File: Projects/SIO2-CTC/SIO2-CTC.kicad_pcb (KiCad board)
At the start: 2 copper layers, 100 x 80 mm, 12 parts, among them IC1 MCP2221-I_P, J1 RetroZ-SBC_ClientBus, J2 Conn_01x08, J3 USB_OTG, U1 74LS138, U2 Z84C3008PEG, U3 Z84C40

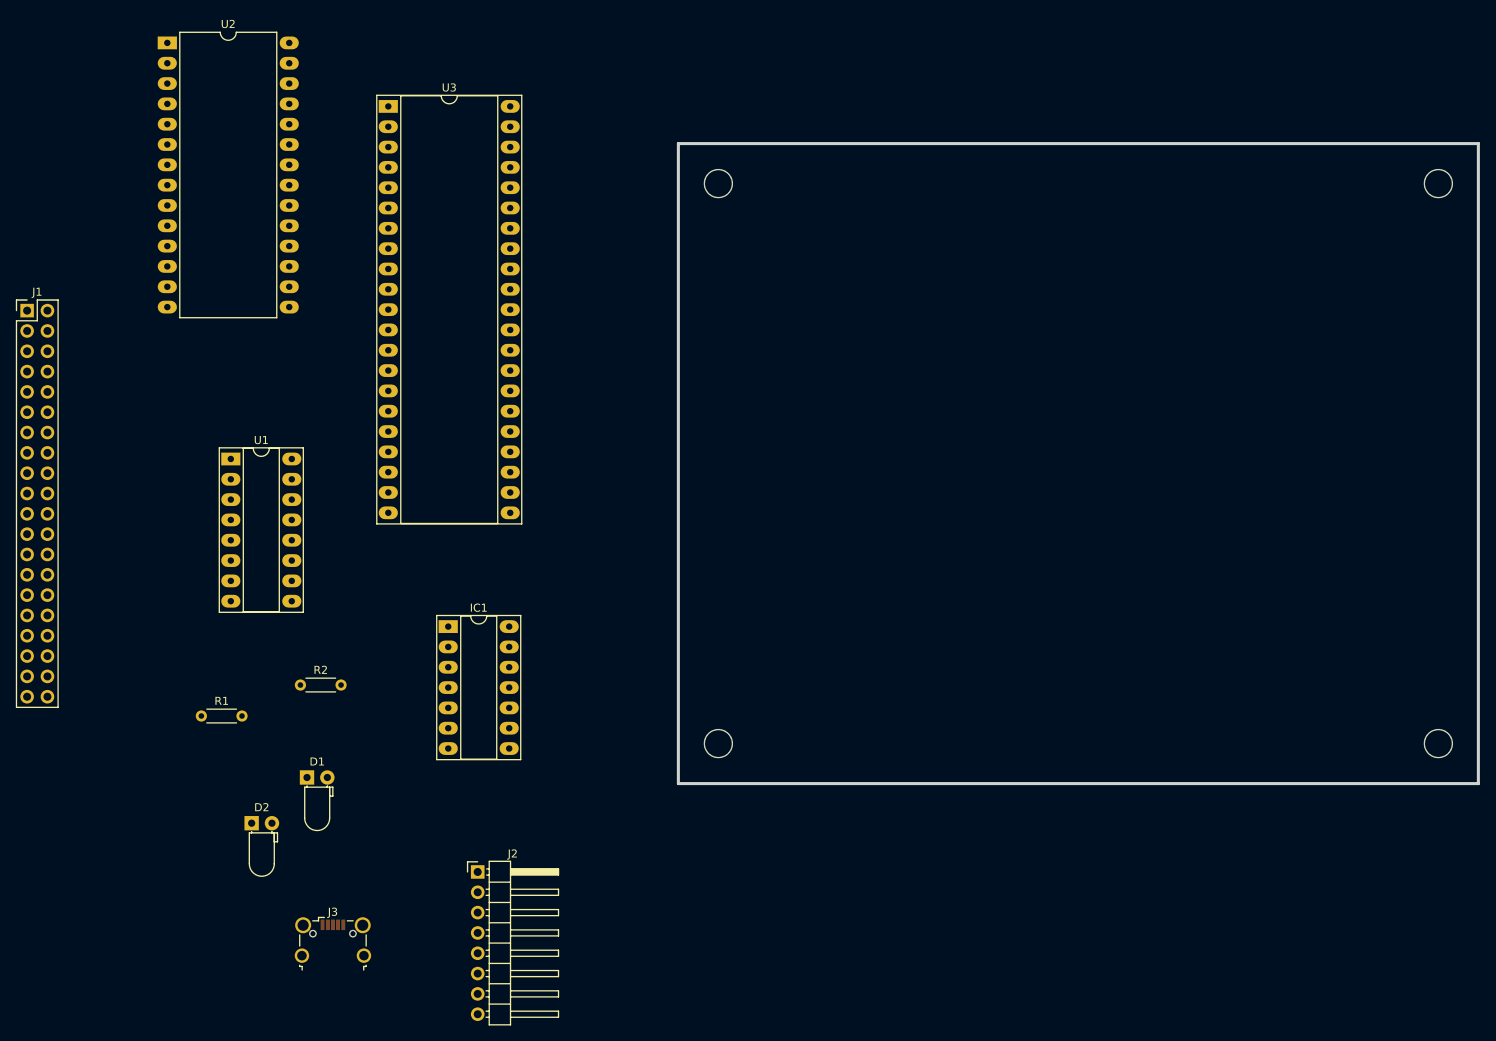
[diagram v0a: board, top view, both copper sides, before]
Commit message: added usb to serial with an FT230XS-U chip
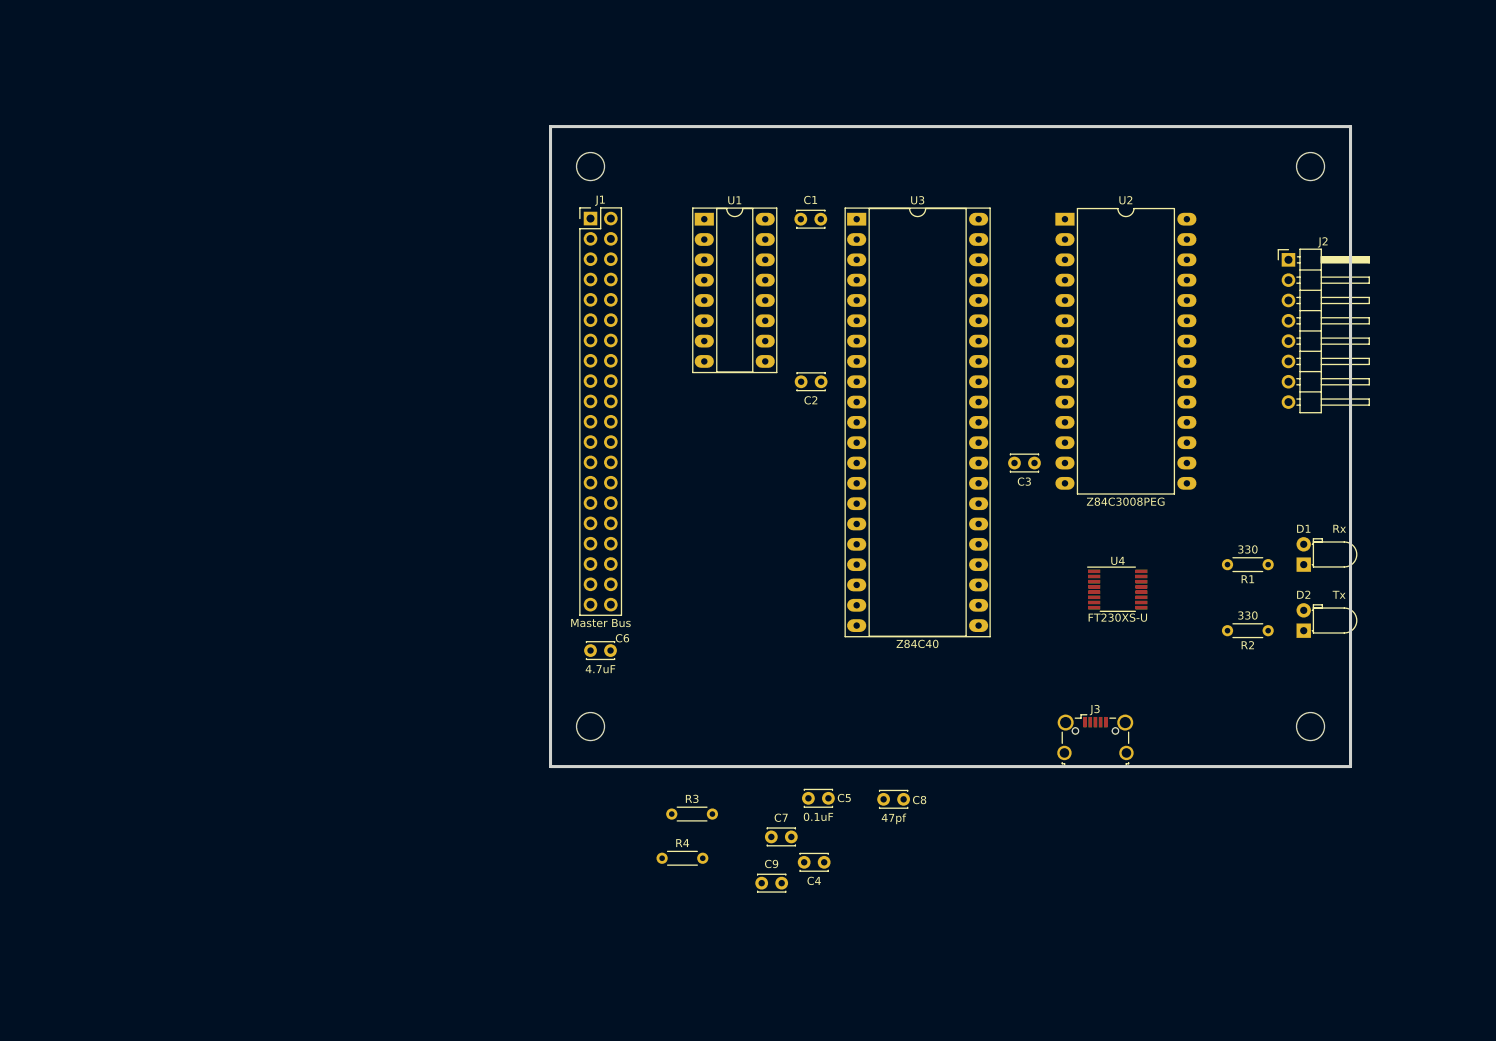
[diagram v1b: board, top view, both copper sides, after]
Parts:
- removed IC1: MCP2221-I_P, Housings_DIP:DIP-14_W7.62mm_Socket_LongPads
- added C1: 0.1uF, Capacitors_THT:C_Disc_D3.4mm_W2.1mm_P2.50mm, F.Cu at (121.3, 68.6)
- added C2: 0.1uF, Capacitors_THT:C_Disc_D3.4mm_W2.1mm_P2.50mm, F.Cu at (123.8, 88.9)
- added C3: 0.1uF, Capacitors_THT:C_Disc_D3.4mm_W2.1mm_P2.50mm, F.Cu at (150.5, 99.1)
- added C4: 0.1uF, Capacitors_THT:C_Disc_D3.4mm_W2.1mm_P2.50mm, F.Cu at (124.2, 149.0)
- added C5: 0.1uF, Capacitors_THT:C_Disc_D3.4mm_W2.1mm_P2.50mm, F.Cu at (122.2, 141.0)
- added C6: 4.7uF, Capacitors_THT:C_Disc_D3.4mm_W2.1mm_P2.50mm, F.Cu at (95.0, 122.5)
- added C7: 0.1uF, Capacitors_THT:C_Disc_D3.4mm_W2.1mm_P2.50mm, F.Cu at (117.6, 145.8)
- added C8: 47pf, Capacitors_THT:C_Disc_D3.4mm_W2.1mm_P2.50mm, F.Cu at (131.6, 141.1)
- added C9: 47pf, Capacitors_THT:C_Disc_D3.4mm_W2.1mm_P2.50mm, F.Cu at (116.4, 151.6)
- added R3: 27, Resistors_THT:R_Axial_DIN0204_L3.6mm_D1.6mm_P5.08mm_Horizontal, F.Cu at (105.2, 142.9)
- added R4: 27, Resistors_THT:R_Axial_DIN0204_L3.6mm_D1.6mm_P5.08mm_Horizontal, F.Cu at (103.9, 148.5)
- added U4: FT230XS-U, Housings_SSOP:TSSOP-16_4.4x5mm_Pitch0.65mm, F.Cu at (160.9, 114.9)
- J1: value RetroZ-SBC_ClientBus -> Master Bus
- moved R1 134.7 mm to (179.7, 111.8), turned to 180 degrees
- moved D2 133.7 mm to (184.2, 120.0), turned to 90 degrees
- moved D1 127.4 mm to (184.2, 111.8), turned to 90 degrees
- moved J2 127.0 mm to (182.2, 73.7)
- moved R2 121.2 mm to (179.7, 120.0), turned to 180 degrees
- moved U2 114.3 mm to (154.3, 68.6)
- moved J3 98.6 mm to (158.1, 133.3)
- moved J1 71.4 mm to (95.0, 68.5)
- moved U1 66.3 mm to (109.2, 68.6)
- moved U3 60.2 mm to (128.3, 68.6)
- moved REF** 16.1 mm to (90.0, 137.0)
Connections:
- J2 pad 2: /GPIO2 -> /CBUS0
- J2 pad 3: /GPIO3 -> /CBUS3
- J3 pad 2: Net-(IC1-Pad12) -> /D-
- J3 pad 3: Net-(IC1-Pad13) -> /D+
- R1 pad 2: Net-(IC1-Pad2) -> /RxLED
- R2 pad 2: Net-(IC1-Pad3) -> /TxLED
- U3 pad 12: Net-(IC1-Pad6) -> /RxA
- U3 pad 15: Net-(IC1-Pad5) -> /TxA
- U3 pad 17: Net-(U3-Pad17) -> /~RTSA
- U3 pad 18: Net-(U3-Pad18) -> /~CTSA
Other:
- net class Default: clearance 0.2 -> 0.1524; trace_width 0.25 -> 0.1524; via_dia 0.6 -> 0.6858; via_drill 0.4 -> 0.3302
- rule trace_clearance: 0.2 -> 0.1524
- rule trace_min: 0.2 -> 0.1524
- rule via_min_drill: 0.3 -> 0.3302
- rule via_min_size: 0.4 -> 0.6858

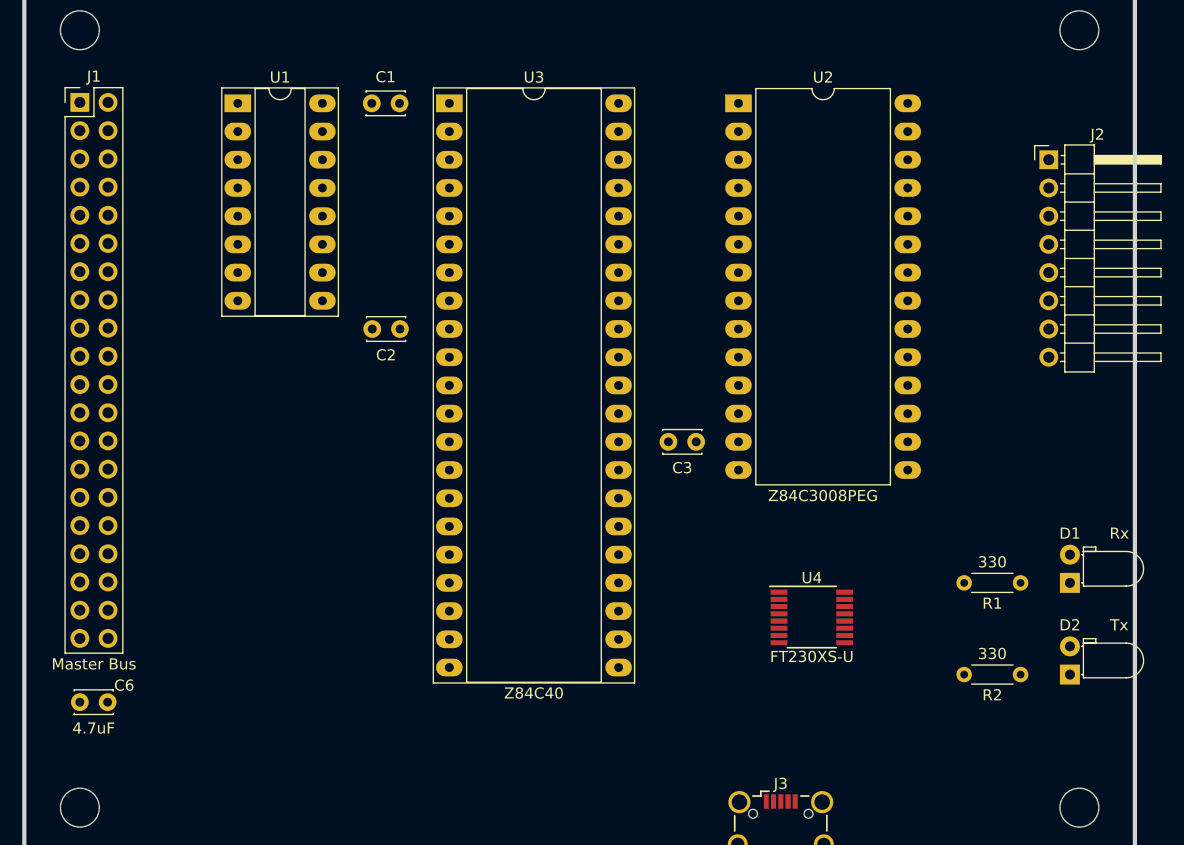
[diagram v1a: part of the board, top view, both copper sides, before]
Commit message: fixed the bus and removed RxTx from the ctc-sio2 board
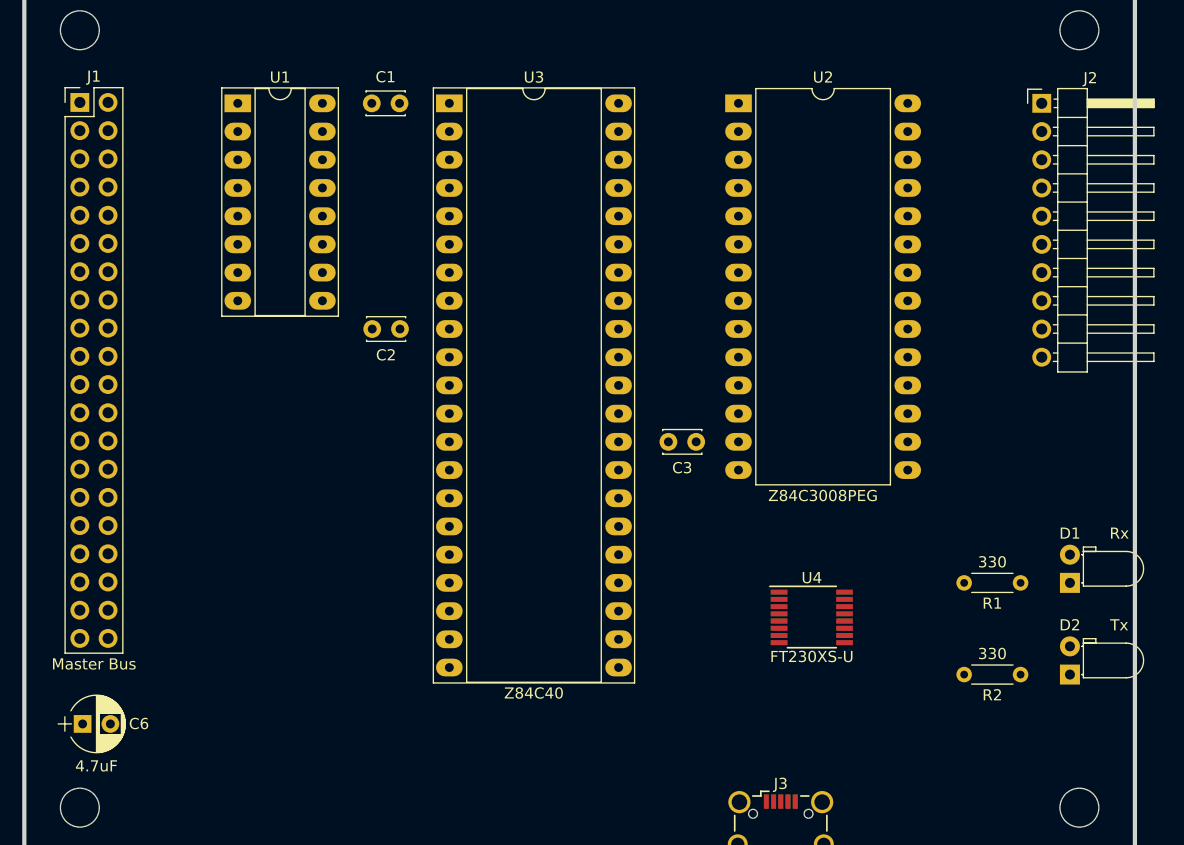
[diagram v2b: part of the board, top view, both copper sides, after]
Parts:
- C6: footprint Capacitors_THT:C_Disc_D3.4mm_W2.1mm_P2.50mm -> Capacitors_THT:CP_Radial_D5.0mm_P2.50mm
- J2: value Conn_01x08 -> Conn_01x10; footprint Pin_Headers:Pin_Header_Angled_1x08_Pitch2.54mm -> Pin_Headers:Pin_Header_Angled_1x10_Pitch2.54mm
- moved J2 5.12 mm to (181.6, 68.6)
- moved C6 1.98 mm to (95.2, 124.5)
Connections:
- net SEL_CTC renamed ~SEL_CTC
- net ~SEL_SIO2 renamed /~SEL_SIO2
- J1 pad 29: Rx -> Net-(J1-Pad29)
- J1 pad 31: Tx -> Net-(J1-Pad31)
- U1 pad 5: GND -> ~IORQ
- U3 pad 26: Tx -> TxB
- U3 pad 29: Rx -> RxB
- U3 pad 30: ~WAIT -> Net-(U3-Pad30)

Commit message: finished sio2 board
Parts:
- removed C5: 0.1uF, Capacitors_THT:C_Disc_D3.4mm_W2.1mm_P2.50mm
- removed C6: 4.7uF, Capacitors_THT:CP_Radial_D5.0mm_P2.50mm
- C1: value 0.1uF -> 4.7uF; footprint Capacitors_THT:C_Disc_D3.4mm_W2.1mm_P2.50mm -> Capacitors_THT:CP_Radial_D5.0mm_P2.50mm
- J1: value Master Bus -> Client Bus
- J2: value Conn_01x10 -> Extension
- moved C4 80.4 mm to (121.3, 68.6), turned to 0 degrees
- moved R4 66.6 mm to (166.4, 125.3), turned to 90 degrees
- moved C7 62.2 mm to (167.0, 108.0)
- moved C1 61.3 mm to (95.0, 124.0)
- moved C9 56.7 mm to (163.6, 120.2), turned to 270 degrees
- moved R3 52.8 mm to (154.9, 125.2), turned to 90 degrees
- moved C8 33.4 mm to (157.7, 120.2), turned to 270 degrees
- moved J3 2.60 mm to (160.7, 133.3)
- moved U4 0.26 mm to (160.7, 114.9)
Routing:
- net ~IORQ: track 0.00 -> 127.1 mm, vias 0 -> 6
- net A0: track 0.00 -> 119.8 mm, vias 0 -> 3
- net A1: track 0.00 -> 117.2 mm, vias 0 -> 2
- net ~RESET: track 0.00 -> 115.6 mm, vias 0 -> 4
- net /D1: track 0.00 -> 110.7 mm, vias 0 -> 4
- net CLK: track 0.00 -> 106.1 mm, vias 0 -> 3
- net /D3: track 0.00 -> 100.7 mm, vias 0 -> 4
- net /D0: track 0.00 -> 98.0 mm, vias 0 -> 4
- net ~M1: track 0.00 -> 95.9 mm, vias 0 -> 4
- net /D2: track 0.00 -> 94.3 mm, vias 0 -> 4
- net ~INT: track 0.00 -> 82.0 mm, vias 0 -> 2
- net ~RD: track 0.00 -> 81.4 mm, vias 0 -> 3
- net /D4: track 0.00 -> 81.2 mm, vias 0 -> 4
- net /D5: track 0.00 -> 79.2 mm, vias 0 -> 4
- net ~SEL_CTC: track 0.00 -> 77.5 mm, vias 0 -> 2
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- added copper zone on B.Cu, net GND
- added copper zone on F.Cu, net VCC
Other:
- board text added: "CBUS0"
- board text added: "CBUS3"
- board text added: "IEO"
- board text added: "RxB"
- board text added: "TO2"
- board text added: "TRG0"
- board text added: "TRG1"
- board text added: "TRG2"
- board text added: "TRG3"
- board text added: "TxB"

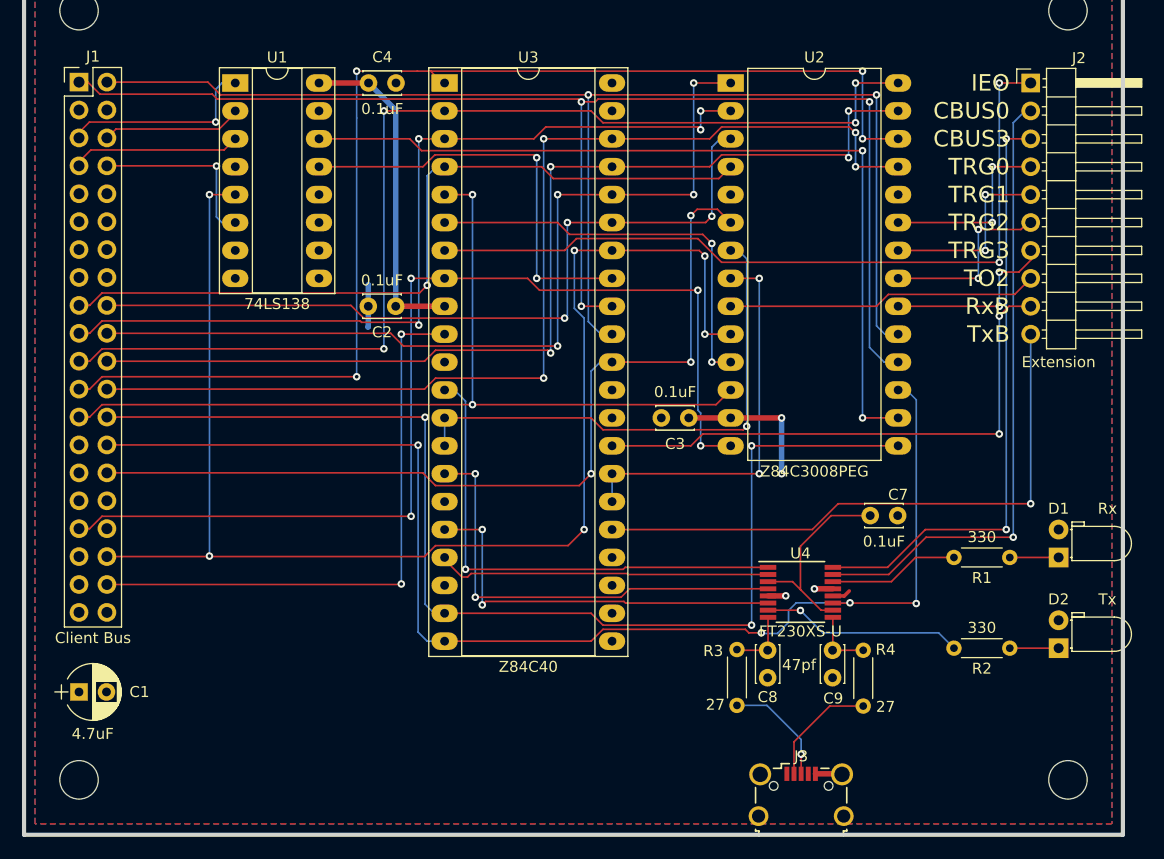
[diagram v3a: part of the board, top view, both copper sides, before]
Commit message: fixed a bunch of issues with the main board and some on the memory board
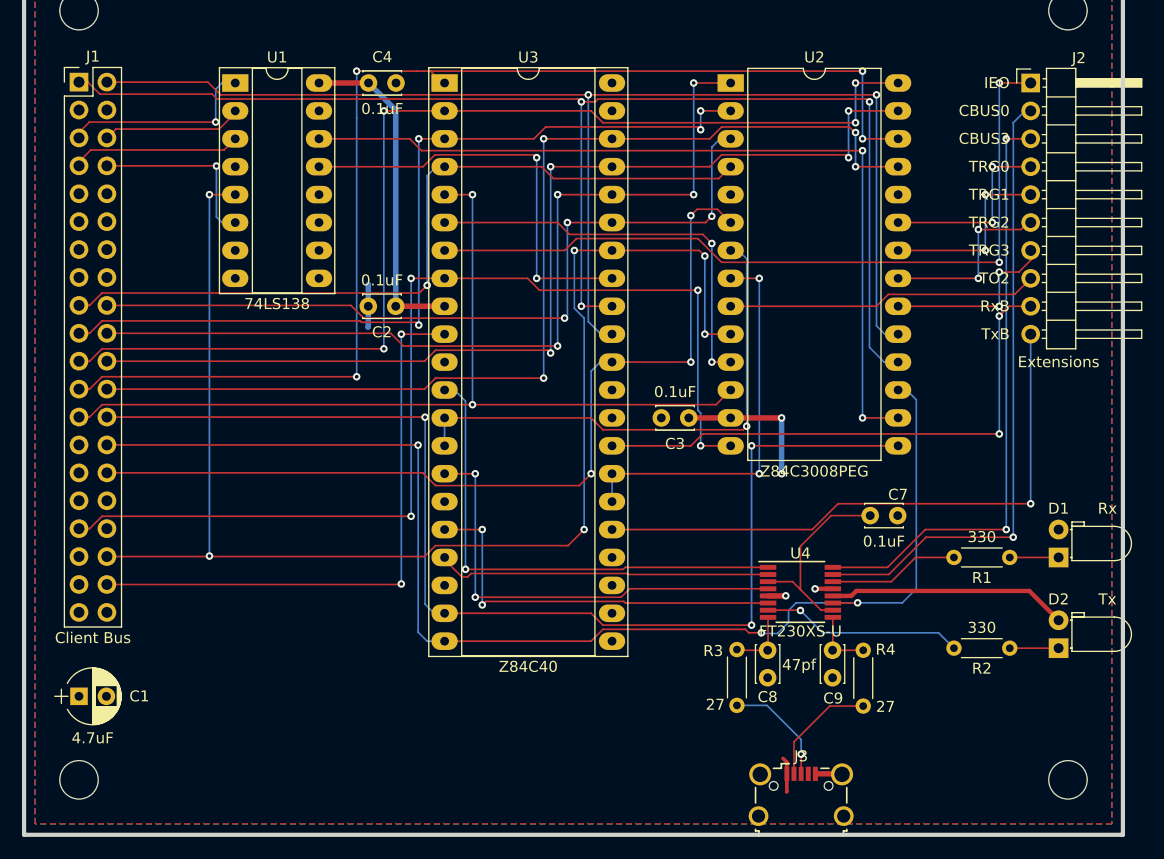
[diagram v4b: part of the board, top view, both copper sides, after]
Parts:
- J2: value Extension -> Extensions
- moved C1 0.40 mm to (95.0, 124.4)
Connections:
- J3 pad 1: Net-(J3-Pad1) -> VCC
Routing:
- net VCC: track 45.5 -> 68.9 mm
- net ~RESET: track 115.6 -> 115.4 mm, vias 4 -> 3

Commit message: completed Main BOM
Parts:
- added REF***: OSHW-Logo_11.4x12mm_SilkScreen, Symbols:OSHW-Logo_11.4x12mm_SilkScreen, F.Cu at (111.9, 101.2)
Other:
- board text added: "RetroZ Stack 2018 SIO/2 + CTC Board Rev. 1 jpgravel@formix.org"
